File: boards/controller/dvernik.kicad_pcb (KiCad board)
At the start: 2 copper layers, 100 x 100 mm, 87 parts, among them P101 WAGO233, P102 CONN_01X06, P103 CONN_01X02, P201 WAGO255, P202 WAGO255, P401 WAGO255, P402 Wago_233-502, P403 Wago_233-502, Q201 2N7002K, Q401 IRFU9024, Q402 IRLML6402, U101 A25L40P, U102 EK-TM4C123GXL, U103 Itead_HC-05, U104 LP2992AIM5-3.3CT-ND, U201 JQX-14FC22CS8-5.0, U202 Cosmo_1010-817, U401 Mini-360, U403 ROE-0505S, U404 HCPL-0601-500E, U405 HCPL-0601-500E, U406 Cosmo_1010-817, U407 SN75176BDR

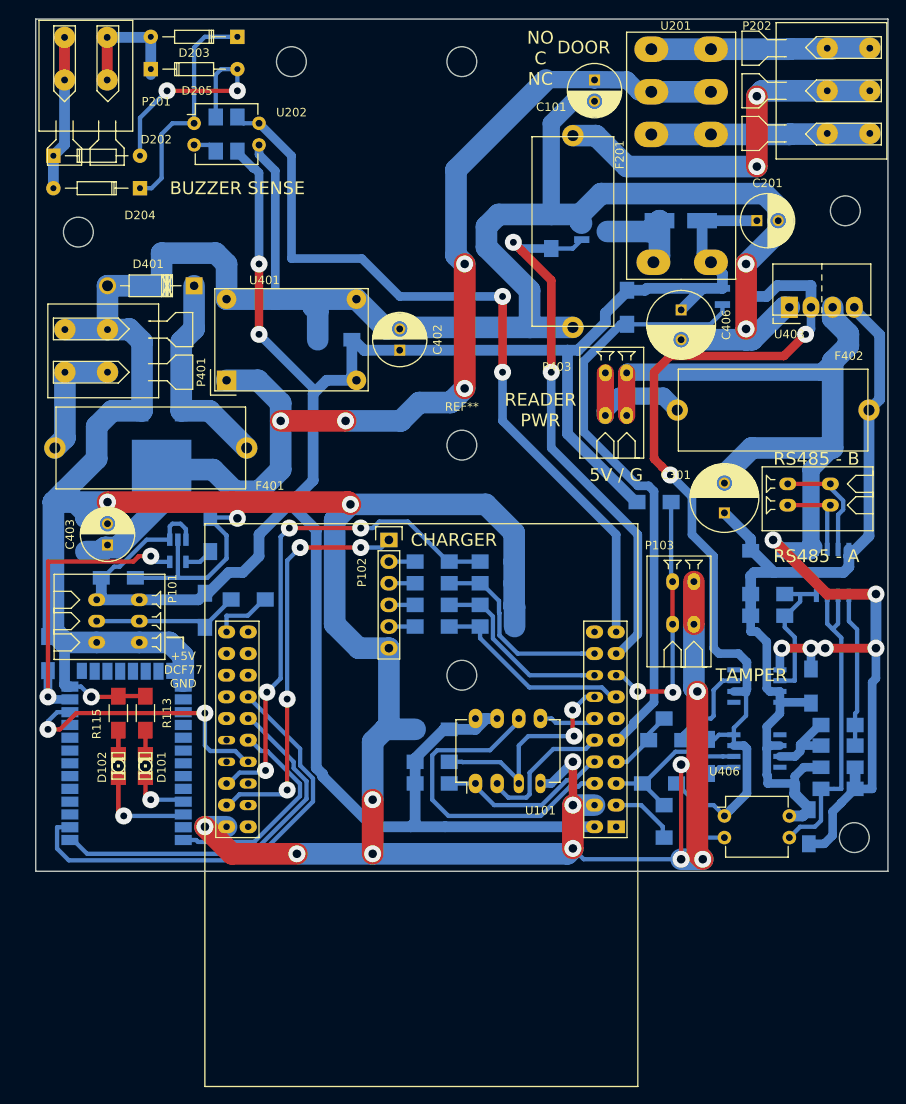
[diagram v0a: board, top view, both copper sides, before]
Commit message: Fix drill sizes, silkscreen and add name and version markings
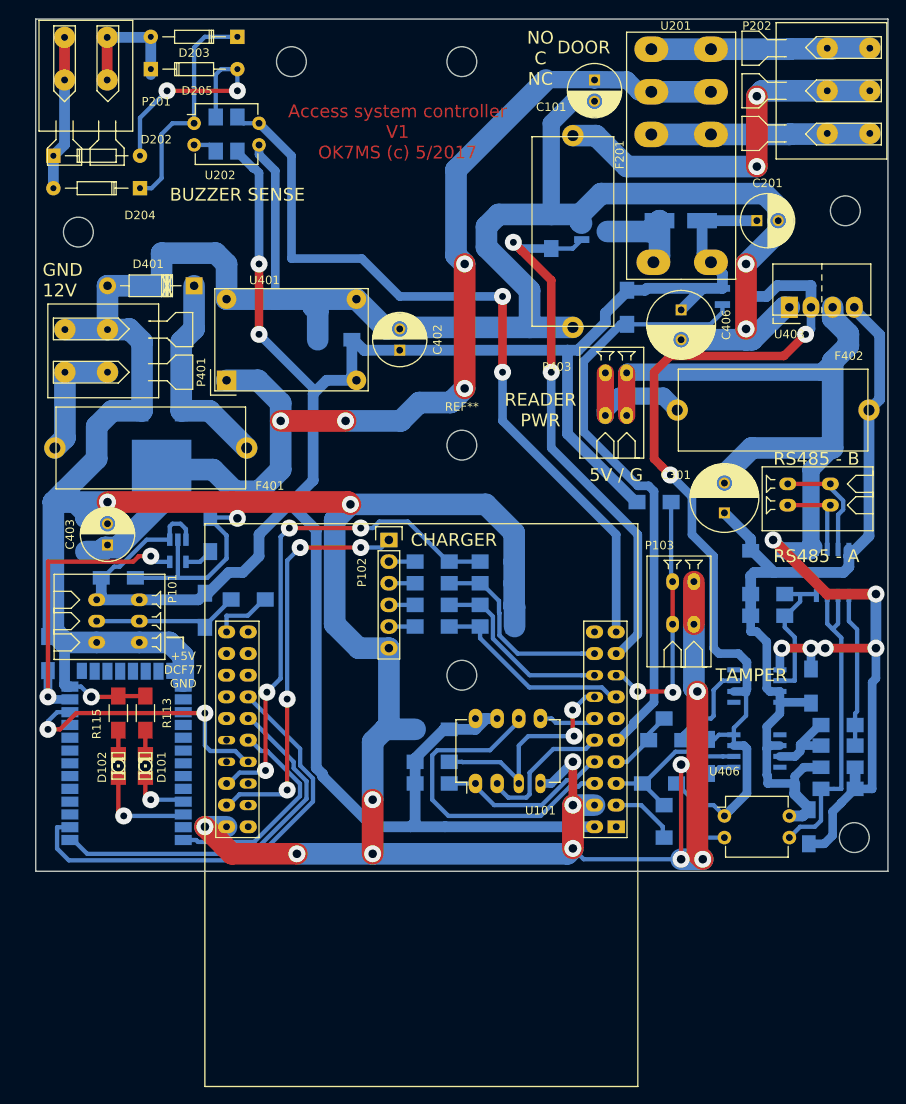
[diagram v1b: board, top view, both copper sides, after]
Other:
- board text added: "Access system controller V1 OK7MS (c) 5/2017"
- board text added: "GND 12V"

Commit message: Add reader board
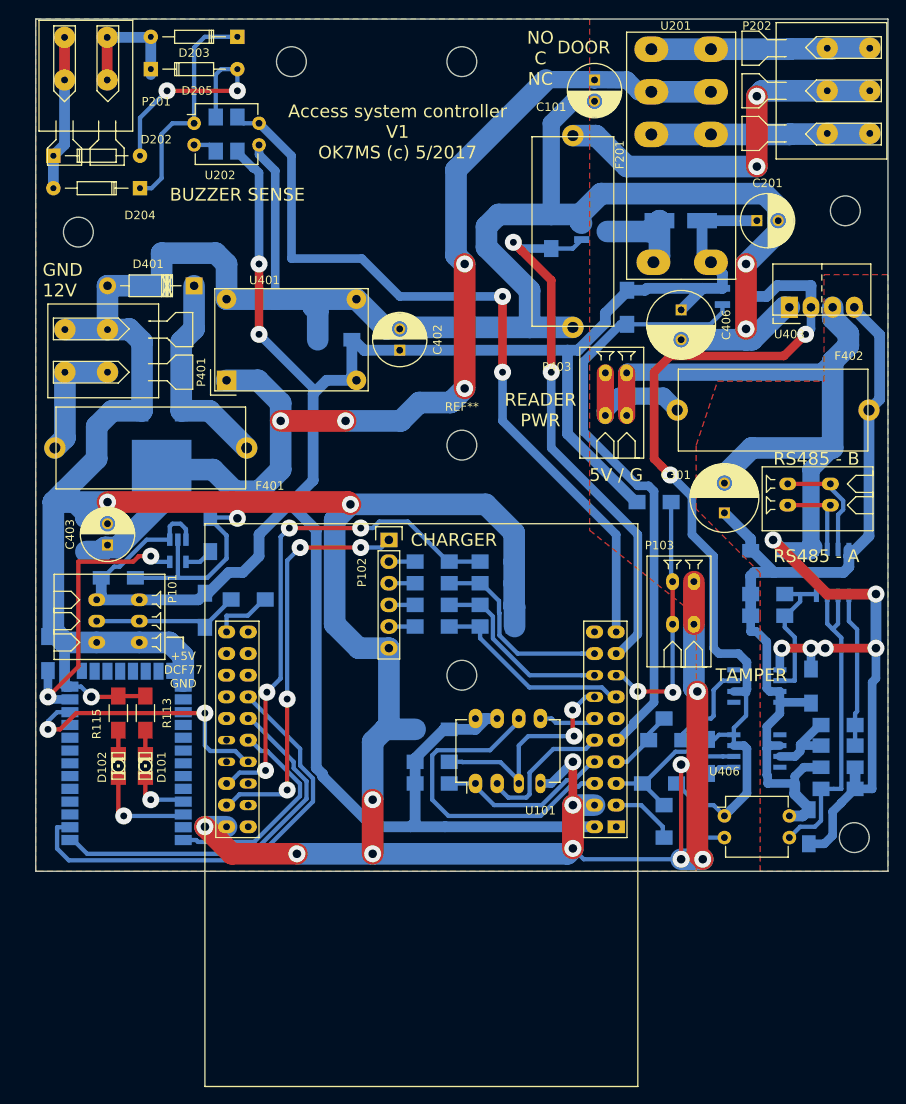
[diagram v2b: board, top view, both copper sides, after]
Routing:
- net Net-(C103-Pad1): track 36.5 -> 34.4 mm
- added copper zone on F.Cu, net GND
- added copper zone on F.Cu, net GNDA
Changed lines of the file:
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@@
-(kicad_pcb (version 20170123) (host pcbnew "(2017-05-14 revision 14bb238)-master")
+(kicad_pcb (version 20170123) (host pcbnew "(2017-05-12 revision b823d0b)-master")
   (general
     (links 194)
@@
     (thickness 1.6)
     (drawings 20)
-    (tracks 773)
+    (tracks 774)
     (zones 0)
     (modules 87)
@@
     (effects (font (size 1.5 1.5) (thickness 0.3)) (justify left))
   )
-  (gr_text "Access system controller\nV1\nOK7MS (c) 5/2017" (at 92.456 63.246) (layer F.Cu)
+  (gr_text "Access system controller\nV1\nOK7MS (c) 5/2017" (at 92.456 63.246) (layer F.SilkS)
     (effects (font (size 1.5 1.5) (thickness 0.3)))
   )
@@
   (segment (start 74.676 137.16) (end 74.93 137.16) (width 0.508) (layer B.Cu) (net 69))
   (via (at 69.85 131.445) (size 2) (drill 0.8) (layers F.Cu B.Cu) (net 69))
-  (segment (start 51.435 113.665) (end 51.435 129.54) (width 0.508) (layer F.Cu) (net 70))
-  (via (at 51.435 129.54) (size 2) (drill 0.8) (layers F.Cu B.Cu) (net 70))
-  (segment (start 61.450787 113.665) (end 51.435 113.665) (width 0.508) (layer F.Cu) (net 70))
   (segment (start 63.5 113.03) (end 62.085787 113.03) (width 0.508) (layer F.Cu) (net 70))
   (segment (start 62.085787 113.03) (end 61.450787 113.665) (width 0.508) (layer F.Cu) (net 70))
+  (segment (start 61.450787 113.665) (end 55 113.665) (width 0.508) (layer F.Cu) (net 70))
+  (segment (start 55 113.665) (end 55 125.975) (width 0.508) (layer F.Cu) (net 70))
+  (segment (start 55 125.975) (end 51.435 129.54) (width 0.508) (layer F.Cu) (net 70))
+  (via (at 51.435 129.54) (size 2) (drill 0.8) (layers F.Cu B.Cu) (net 70))
   (segment (start 65.725 113.695) (end 64.165 113.695) (width 0.508) (layer B.Cu) (net 70))
   (segment (start 64.165 113.695) (end 63.5 113.03) (width 0.508) (layer B.Cu) (net 70))
@@
   (segment (start 143.24 105.015906) (end 143.24 104.545) (width 0.508) (layer B.Cu) (net 74))
   (segment (start 144.74801 107.566084) (end 144.74801 106.523916) (width 0.508) (layer B.Cu) (net 74))
+  (zone (net 1) (net_name GND) (layer F.Cu) (hatch edge 0.508)
+    (connect_pads (clearance 0.508))
+    (min_thickness 0.254)
+    (fill yes (arc_segments 16) (thermal_gap 0.508) (thermal_bridge_width 0.508))
+    (polygon
+      (pts
+        (xy 50 50) (xy 115 50) (xy 115 110) (xy 127.5 120) (xy 127.5 150)
+        (xy 50 150)
+      )
+    )
+  )
+  (zone (net 5) (net_name GNDA) (layer F.Cu) (hatch edge 0.508)
+    (connect_pads (clearance 0.508))
+    (min_thickness 0.254)
+    (fill yes (arc_segments 16) (thermal_gap 0.508) (thermal_bridge_width 0.508))
+    (polygon
+      (pts
+        (xy 150 150) (xy 135 150) (xy 135 120) (xy 135 115) (xy 127.5 107.5)
+        (xy 127.5 100) (xy 130 92.5) (xy 142.5 92.5) (xy 142.5 80) (xy 150 80)
+      )
+    )
+  )
 )
